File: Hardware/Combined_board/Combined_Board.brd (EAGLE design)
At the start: 44.5 x 118.7 mm, 19 parts, among them IC1 788TV, M1 SERVO, M2 SERVO, U1 BMI088

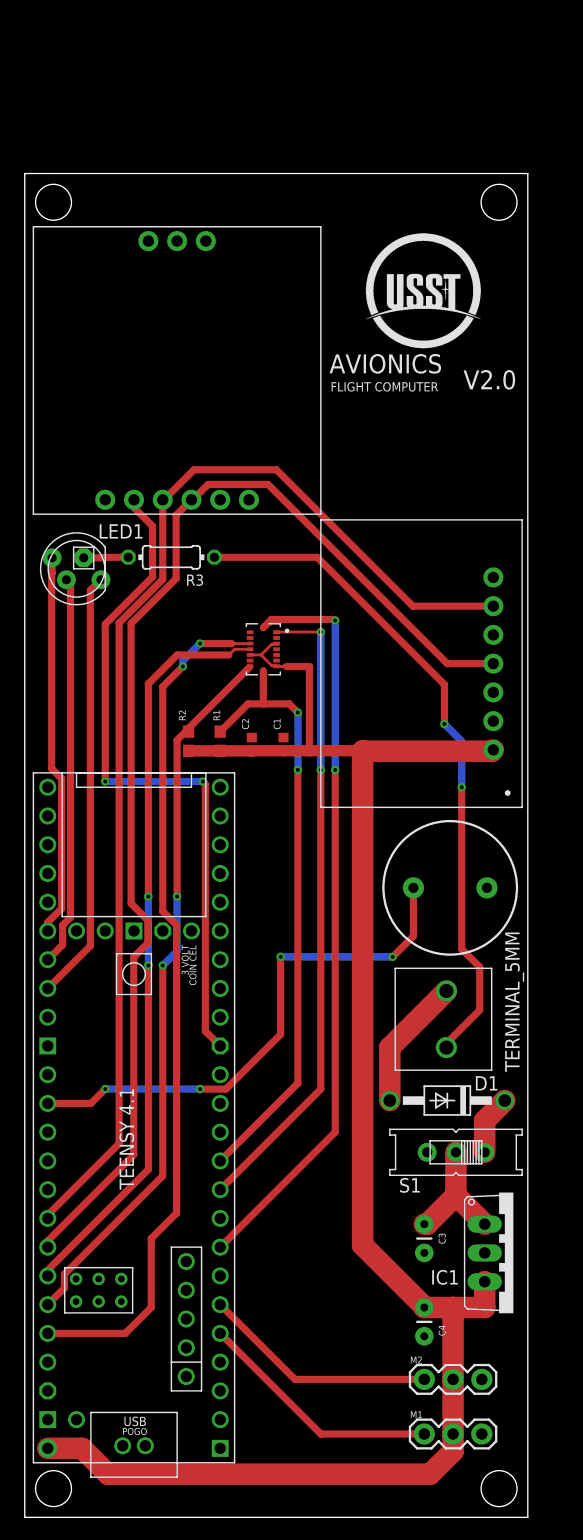
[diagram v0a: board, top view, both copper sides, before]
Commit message: added mosfets to combine boards (#56)
* Combined Avionics board and BMI088 board into on PCB named Combined Board, added space for plunger to fit around the combined board. Changed Avionics board to include a diode and power switch.

* added mosfet to combine boards
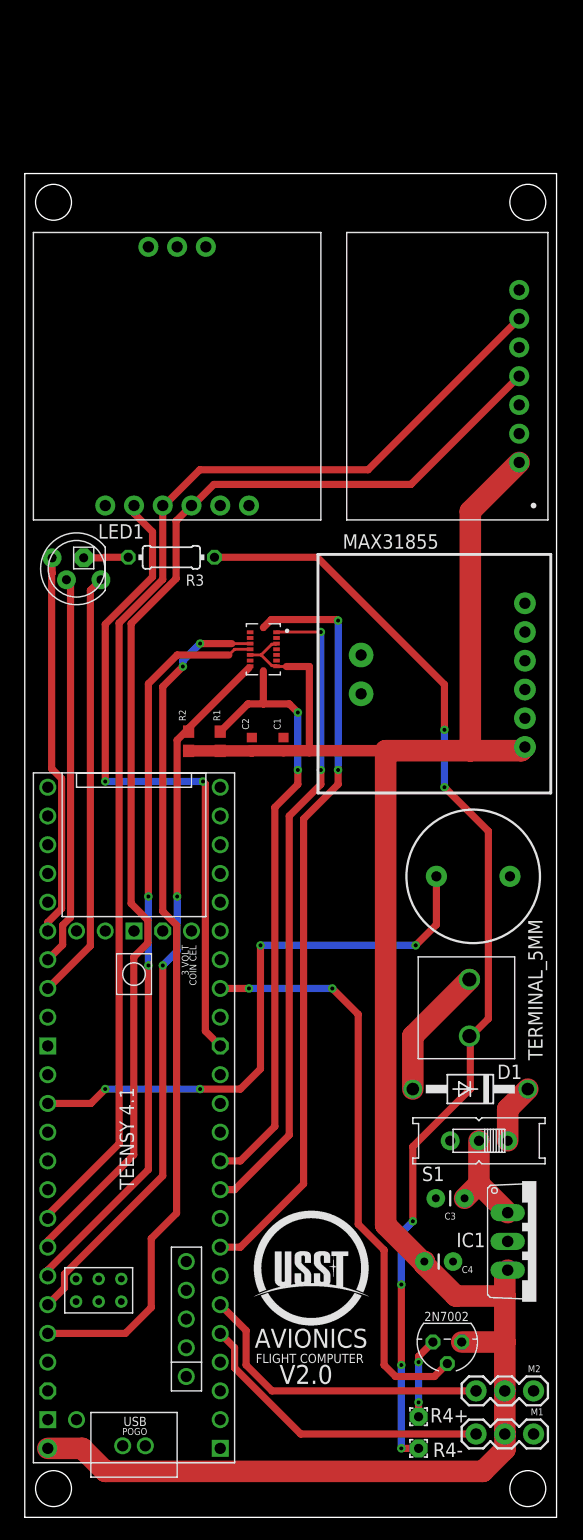
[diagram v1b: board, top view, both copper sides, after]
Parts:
- added 2N7002: 2N3819, transistor-fet:TO92
- added R4+, R4-: (no value), wirepad:1,6/0,8
- added U$2: MAX31855, max31855:MAX31855-BREAKOUT
- moved BMP1 25.5 mm to (46.2, 88.1)
- moved C4 5.48 mm to (36.6, 22.6), turned to 0 degrees
- moved M2 4.68 mm to (39.9, 11.2)
- moved M1 4.57 mm to (39.9, 7.37)
- moved C3 4.23 mm to (37.6, 28.2), turned to 180 degrees
- moved LS1 2.27 mm to (39.6, 56.6)
- moved IC1 2.27 mm to (45.2, 24.4)
- moved D1 2.27 mm to (39.4, 37.8)
- moved S1 2.27 mm to (40.1, 33.3)
- moved TERMINAL 2.27 mm to (34.3, 49.5)
- moved U$4 0.51 mm to (0.76, 88.1)
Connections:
- new net HEADER11: 2N7002.2, U$1.25-A11/RX6/SDA2
- new net N$3: 2N7002.1, R4+.1
- net 5V: now also 2N7002.3, U$2.+5V
- net GND: now also R4-.1
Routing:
- net HEADER11: track 0.00 -> 51.6 mm, vias 0 -> 2
- net GND: track 59.6 -> 98.9 mm, vias 2 -> 6
- net 5V: track 151.7 -> 189.5 mm
- net N$3: track 0.00 -> 7.13 mm, vias 0 -> 2
- net TVCY: track 20.8 -> 27.5 mm
- net TVCX: track 21.7 -> 27.3 mm
- net BUZZER: track 46.7 -> 51.6 mm
- net SDA: track 103.0 -> 105.5 mm
- net 12V: track 11.2 -> 9.20 mm
- net HEADER2: track 66.3 -> 67.7 mm
- net HEADER5: track 53.6 -> 54.6 mm
- net HEADER4: track 56.9 -> 57.6 mm
- net SCL: track 106.3 -> 105.7 mm
- net 3V3: track 59.9 -> 59.4 mm
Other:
- board size 44.5 x 118.7 mm -> 47 x 118.7 mm

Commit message: Updated flight computer to new version for mini rockets
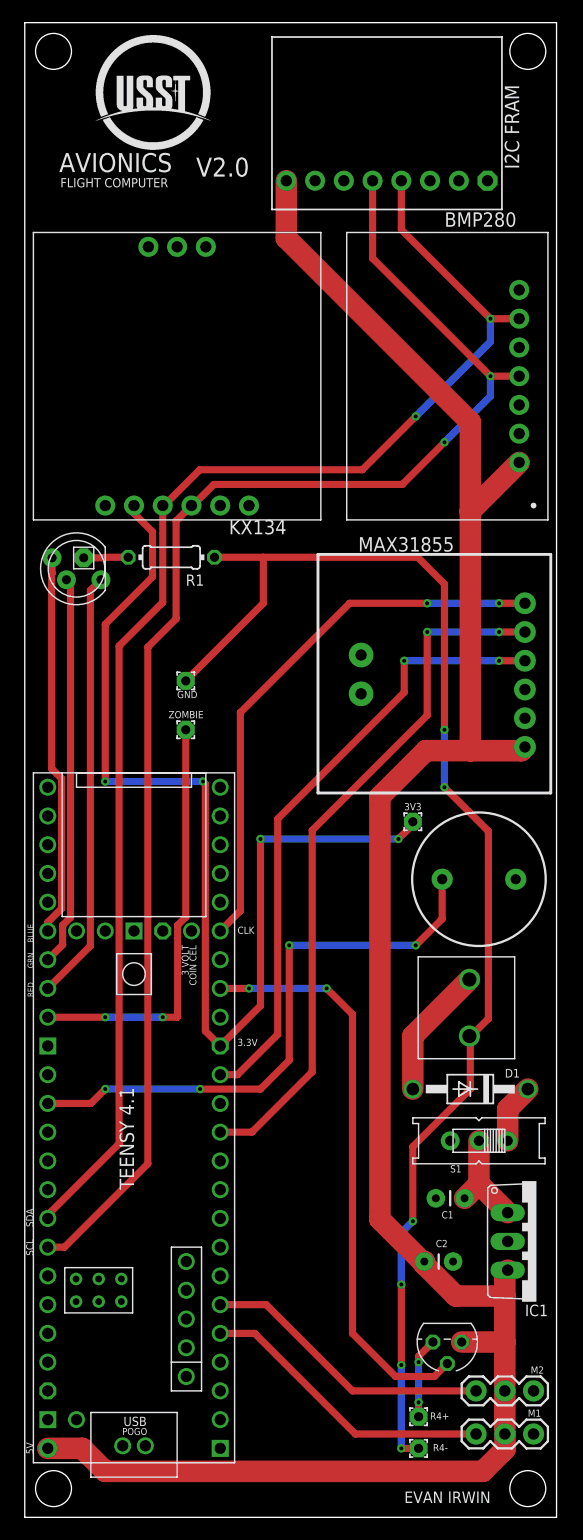
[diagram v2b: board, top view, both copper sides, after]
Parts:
- removed C3: 1uF, SparkFun-Capacitors:CAP-PTH-2.54
- removed C4: 10uF, SparkFun-Capacitors:CAP-PTH-2.54
- removed R2: 0.1, SparkFun-Resistors:0603
- removed R3: 220, rcl:0204/7
- removed U1: BMI088, BMI088:PQFN50P450X300X100-16N
- added 3V, GND, ZOMBIE: 0, wirepad:1,6/0,8
- added U$3: I2CFRAM, I2CFRAM:I2CFRAM
- C1: value 0.1uF -> 1uF; device SparkFun-Capacitors:0402 -> SparkFun-Capacitors:CAP-PTH-2.54
- C2: value 0.1uF -> 10uF; device SparkFun-Capacitors:0402 -> SparkFun-Capacitors:CAP-PTH-2.54
- R1: value 0.1 -> 220; device SparkFun-Resistors:0603 -> rcl:0204/7
- R4+, R4-: value (none) -> 0
- moved C2 48.6 mm to (36.6, 22.6), turned to 0 degrees
- moved C1 42.8 mm to (37.6, 28.2), turned to 180 degrees
- moved R1 16.8 mm to (13.0, 84.8), turned to 0 degrees
- moved LS1 0.57 mm to (40.1, 56.4)
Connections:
- removed net HEADER1: U$1.5-IN2
- removed net HEADER10: U$1.24-A10/TX6/SCL2
- removed net HEADER2: U$1.6-OUT1D, U1.16
- removed net HEADER3: U$1.7-RX2/OUT1A
- removed net HEADER4: U$1.8-TX2/IN2, U1.1
- removed net HEADER5: R1.2, U$1.9-OUT1C, U1.8
- removed net HEADER6: U$1.20-A6/TX5/LRCLK1, U1.12
- removed net HEADER7: R2.2, U$1.21-A7/RX5/BCLK1, U1.9
- removed net HEADER8: U$1.22-A8/CTX1, U1.13
- removed net HEADER9: U$1.23-A9/CRX1/MCLK1
- removed net MOSI: U$1.11-MOSI/CTX1
- removed net SCK: U$1.13-SCK/LED
- new net CLK: U$1.27-A13/SCK1, U$2.CLK
- new net ZOMBIE: U$1.41-A17/MISO1, ZOMBIE.1
- net 12V: now also C1.1; no longer C3.1
- net 3V3: now also 3V.1
- net 5V: now also U$3.VCC; no longer C1.1, C4.1, R1.1, R2.1, U1.11, U1.3, U1.7
- net CS: now also U$2.CS
- net GND: now also GND.1, R1.2, U$2.GND; no longer C3.2, C4.2, R3.2, U1.2, U1.4, U1.6
- net MISO: now also U$2.DO
- net N$1: now also R1.1; no longer R3.1
- net SCL: now also U$3.SCL
- net SDA: now also U$3.SDA
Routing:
- net HEADER8: track 76.2 -> 0.00 mm, vias 2 -> 0
- net HEADER2: track 67.7 -> 0.00 mm, vias 2 -> 0
- net HEADER6: track 66.3 -> 0.00 mm, vias 2 -> 0
- net HEADER7: track 64.1 -> 0.00 mm, vias 2 -> 0
- net CS: track 0.00 -> 62.0 mm, vias 0 -> 2
- net HEADER4: track 57.6 -> 0.00 mm, vias 2 -> 0
- net MISO: track 0.00 -> 54.9 mm, vias 0 -> 2
- net HEADER5: track 54.6 -> 0.00 mm, vias 2 -> 0
- net CLK: track 0.00 -> 49.2 mm, vias 0 -> 2
- net ZOMBIE: track 0.00 -> 37.1 mm, vias 0 -> 2
- net 3V3: track 59.4 -> 93.4 mm, vias 2 -> 4
- net SCL: track 105.7 -> 128.0 mm, vias 0 -> 2
- net GND: track 98.9 -> 117.9 mm
- net SDA: track 105.5 -> 122.2 mm, vias 0 -> 2
- net TVCY: track 27.5 -> 25.8 mm
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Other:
- board size 47 x 118.7 mm -> 47 x 132.1 mm
- board text added: "3.3V"
- board text added: "3V3"
- board text added: "5V"
- board text added: "BLUE"
- board text added: "BMP280"
- board text added: "C1"
- board text added: "C2"
- board text added: "CLK"
- board text added: "D1"
- board text added: "EVAN IRWIN"
- board text added: "GND"
- board text added: "GRN"
- board text added: "I2C FRAM"
- board text added: "IC1"
- board text added: "KX134"
- board text added: "M1"
- board text added: "M2"
- board text added: "MAX31855"
- board text added: "RED"
- board text added: "S1"
- board text added: "SCL"
- board text added: "SDA"
- board text added: "ZOMBIE"
